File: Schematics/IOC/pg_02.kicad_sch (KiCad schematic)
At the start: 7 parts, among them U301 68020, U302 F260, U303 F260, U304 F51, U305 F02, U306 F20

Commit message: Align to grid
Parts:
- removed GB7: GB, symbol r1000:GB
- removed U301: 68020, symbol r1000:68020
- removed U302, U303: F260, symbol r1000:F260
- removed U304: F51, symbol r1000:F51
- removed U305: F02, symbol r1000:F02
- removed U306: F20, symbol r1000:F20
- added U: (no value), symbol r1000:GB
- added U: (no value), symbol r1000:F20
- added U (x2): (no value), symbol r1000:F260
- added U: (no value), symbol r1000:F51
- added U: (no value), symbol r1000:F02
- added U: (no value), symbol r1000:68020
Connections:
- net 68K.A0: now also U.C4 (A00)
- net 68K.A1: now also U.A2 (A01)
- net 68K.A10: now also U.B12 (A10)
- net 68K.A11: now also U.A12 (A11)
- net 68K.A12: now also U.C10 (A12)
- net 68K.A13: now also U.B11 (A13)
- net 68K.A14: now also U.A19 (A14)
- net 68K.A15: now also U.B10 (A15)
- net 68K.A16: now also U.C9 (A16)
- net 68K.A17: now also U.C8 (A17)
- net 68K.A18: now also U.B8 (A18)
- net 68K.A19: now also U.A8 (A19)
- net 68K.A2: now also U.E12 (A02)
- net 68K.A20: now also U.B7 (A20)
- net 68K.A21: now also U.C7 (A21)
- net 68K.A22: now also U.A7 (A22)
- net 68K.A23: now also U.A6 (A23)
- net 68K.A24: now also U.B6 (A24)
- net 68K.A25: now also U.C6 (A25)
- net 68K.A26: now also U.A5 (A26)
- net 68K.A27: now also U.B5 (A27)
- net 68K.A28: now also U.A4 (A28)
- net 68K.A29: now also U.C5 (A29)
- net 68K.A3: now also U.D13 (A03)
- net 68K.A30: now also U.B4 (A30)
- net 68K.A31: now also U.A3 (A31)
- net 68K.A4: now also U.D12 (A04)
- net 68K.A5: now also U.C13 (A05)
- net 68K.A6: now also U.B13 (A06)
- net 68K.A7: now also U.C12 (A07)
- net 68K.A8: now also U.A13 (A08)
- net 68K.A9: now also U.C11 (A09)
- net 68K.BERR~: now also U.7 (Q), U.J2 (BERR)
- net 68K.D0: now also U.K13 (D00)
- net 68K.D1: now also U.K12 (D01)
- net 68K.D10: now also U.M10 (D10)
- net 68K.D11: now also U.L9 (D11)
- net 68K.D12: now also U.N10 (D12)
- net 68K.D13: now also U.M9 (D13)
- net 68K.D14: now also U.N9 (D14)
- net 68K.D15: now also U.L8 (D15)
- net 68K.D16: now also U.M7 (D16)
- net 68K.D17: now also U.N6 (D17)
- net 68K.D18: now also U.M6 (D18)
- net 68K.D19: now also U.L6 (D19)
- net 68K.D2: now also U.L13 (D02)
- net 68K.D20: now also U.N5 (D20)
- net 68K.D21: now also U.M5 (D21)
- net 68K.D22: now also U.N4 (D22)
- net 68K.D23: now also U.L5 (D23)
- net 68K.D24: now also U.M4 (D24)
- net 68K.D25: now also U.N3 (D25)
- net 68K.D26: now also U.M3 (D26)
- net 68K.D27: now also U.L4 (D27)
- net 68K.D28: now also U.N2 (D28)
- net 68K.D29: now also U.M2 (D29)
- net 68K.D3: now also U.L12 (D03)
- net 68K.D30: now also U.L3 (D30)
- net 68K.D31: now also U.N1 (D31)
- net 68K.D4: now also U.M13 (D04)
- net 68K.D5: now also U.M12 (D05)
- net 68K.D6: now also U.M11 (D06)
- net 68K.D7: now also U.L10 (D07)
- net 68K.D8: now also U.N12 (D08)
- net 68K.D9: now also U.N11 (D09)
- net 68K.DSACK0~: now also U.5 (Q), U.H3 (DSACK0)
- net 68K.DSACK1~: now also U.5 (Q), U.J1 (DSACK1)
- net 68K.FC0: now also U.E1 (FC0)
- net 68K.FC1: now also U.F3 (FC1)
- net 68K.FC2: now also U.F2 (FC2)
- net 68K_RESET~: now also U.C1 (RESET)
- net AS~: now also U.L1 (AS)
- net CLK.2X.B5: now also U.C2 (CLK)
- net DBEN~: now also U.G3 (DBEN)
- net DEV.DSACK0: now also U.12 (D0)
- net DEV.DSACK1: now also U.12 (D0)
- net ECS~: now also U.G1 (ECS)
- net IACK_DSACK: now also U.1 (D2)
- net IO.BERRA~: now also U.1 (D0)
- net IO.BERRD~: now also U.2 (D1)
- net IO.DSACK: now also U.1 (D2)
- net IOP.BERR_EN: now also U.1 (A1)
- net IOP.PROT_BERR~: now also U.4 (D2)
- net IOP.RAM_DSACK: now also U.13 (D1), U.13 (D1)
- net IOP_CACHE_EN: now also U.1, U.H1 (CDIS)
- net IOP_HALT: now also U.3 (Q)
- net IPL0~: now also U.J12 (IPL0)
- net IPL1~: now also U.J13 (IPL1)
- net IPL2~: now also U.H12 (IPL2)
- net PD: now also U.2 (D3), U.2 (D3), U.3 (D4), U.3 (D4)
- net PU: now also U.1 (D0), U.2 (D1), U.3 (A3), U.4 (B1), U.5 (D3), U.6 (B3), U.A1 (BGACK), U.B3 (BR), U.H2 (AVEC), U.K2 (HALT)
- net RAM.PERR: now also U.2 (A2)
- net SIZ0: now also U.F1 (SIZ0)
- net SIZ1: now also U.G2 (SIZ1)
- net WR~: now also U.L2 (WR)
- new net: U.5 (B2), U.6 (Q)

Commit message: TYP/VAL busses
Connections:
- net PU: no longer U.K2 (HALT)
- no-connect marks 5 -> 6
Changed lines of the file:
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@@
   (junction (at 114.3 160.02) (diameter 0) (color 0 0 0 0)
   )
-  (junction (at 223.52 66.04) (diameter 0) (color 0 0 0 0)
-  )
   (junction (at 111.76 210.82) (diameter 0) (color 0 0 0 0)
   )
@@
   (junction (at 111.76 215.9) (diameter 0) (color 0 0 0 0)
   )
+  (no_connect (at 231.14 109.22))
   (no_connect (at 312.42 114.3))
   (no_connect (at 312.42 93.98))
@@
     (stroke (width 0) (type default))
   )
-  (wire (pts (xy 223.52 109.22) (xy 223.52 66.04))
-    (stroke (width 0) (type default))
-  )
   (bus (pts (xy 383.54 274.32) (xy 383.54 279.4))
     (stroke (width 0) (type default))
@@
     (stroke (width 0) (type default))
   )
-  (wire (pts (xy 231.14 109.22) (xy 223.52 109.22))
-    (stroke (width 0) (type default))
-  )

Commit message: IOC: dedup, clocks, dfsm
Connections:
- net CLK.2X.B5 renamed CLK.2X
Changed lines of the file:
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@@
     )
   )
-  (global_label "CLK.2X.B5" (shape input) (at 93.98 99.06 180) (fields_autoplaced)
+  (global_label "CLK.2X" (shape input) (at 93.98 99.06 180) (fields_autoplaced)
     (effects (font (size 2.54 2.54)) (justify right))
     (property "Intersheet References" "${INTERSHEET_REFS}" (id 0) (at 69.4206 98.9013 0)

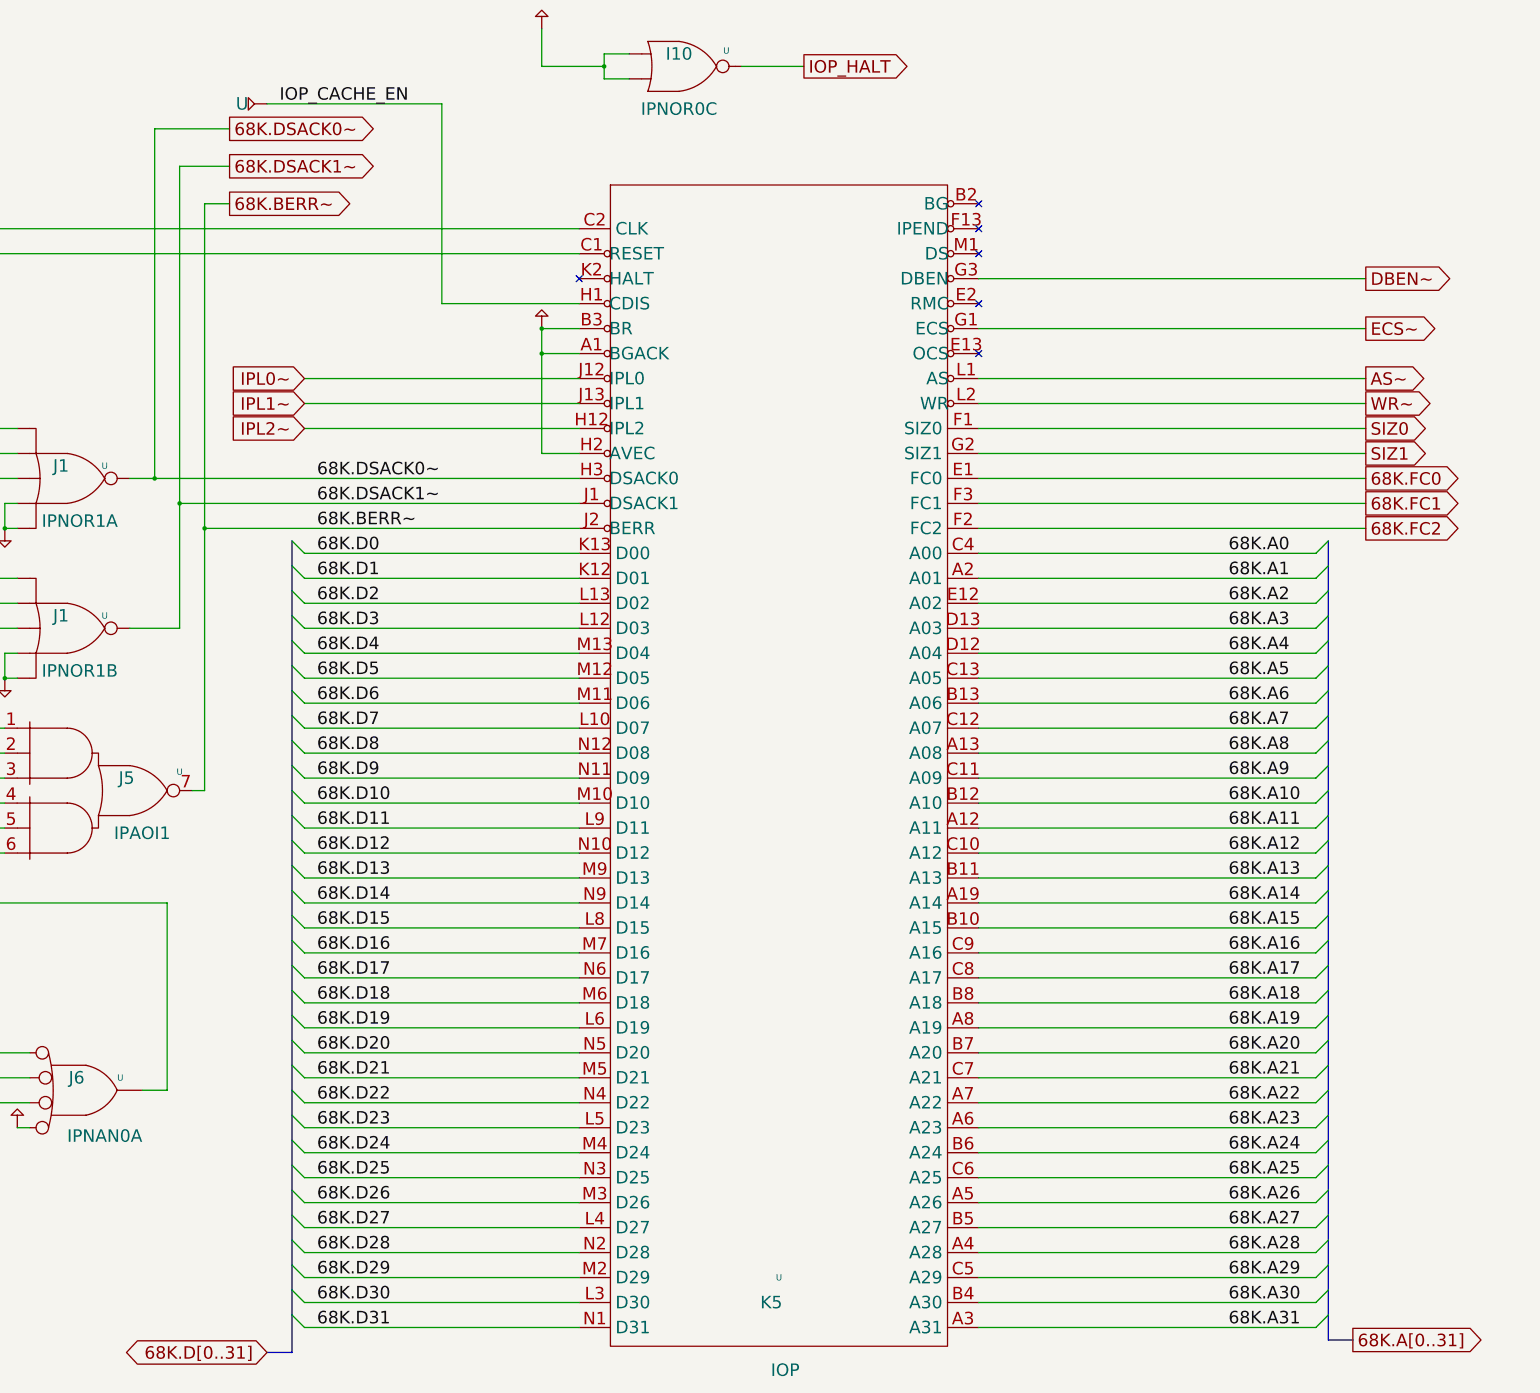
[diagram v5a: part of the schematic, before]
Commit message: IOC/RESHA cleanup, tested to 6 seconds (@c11)
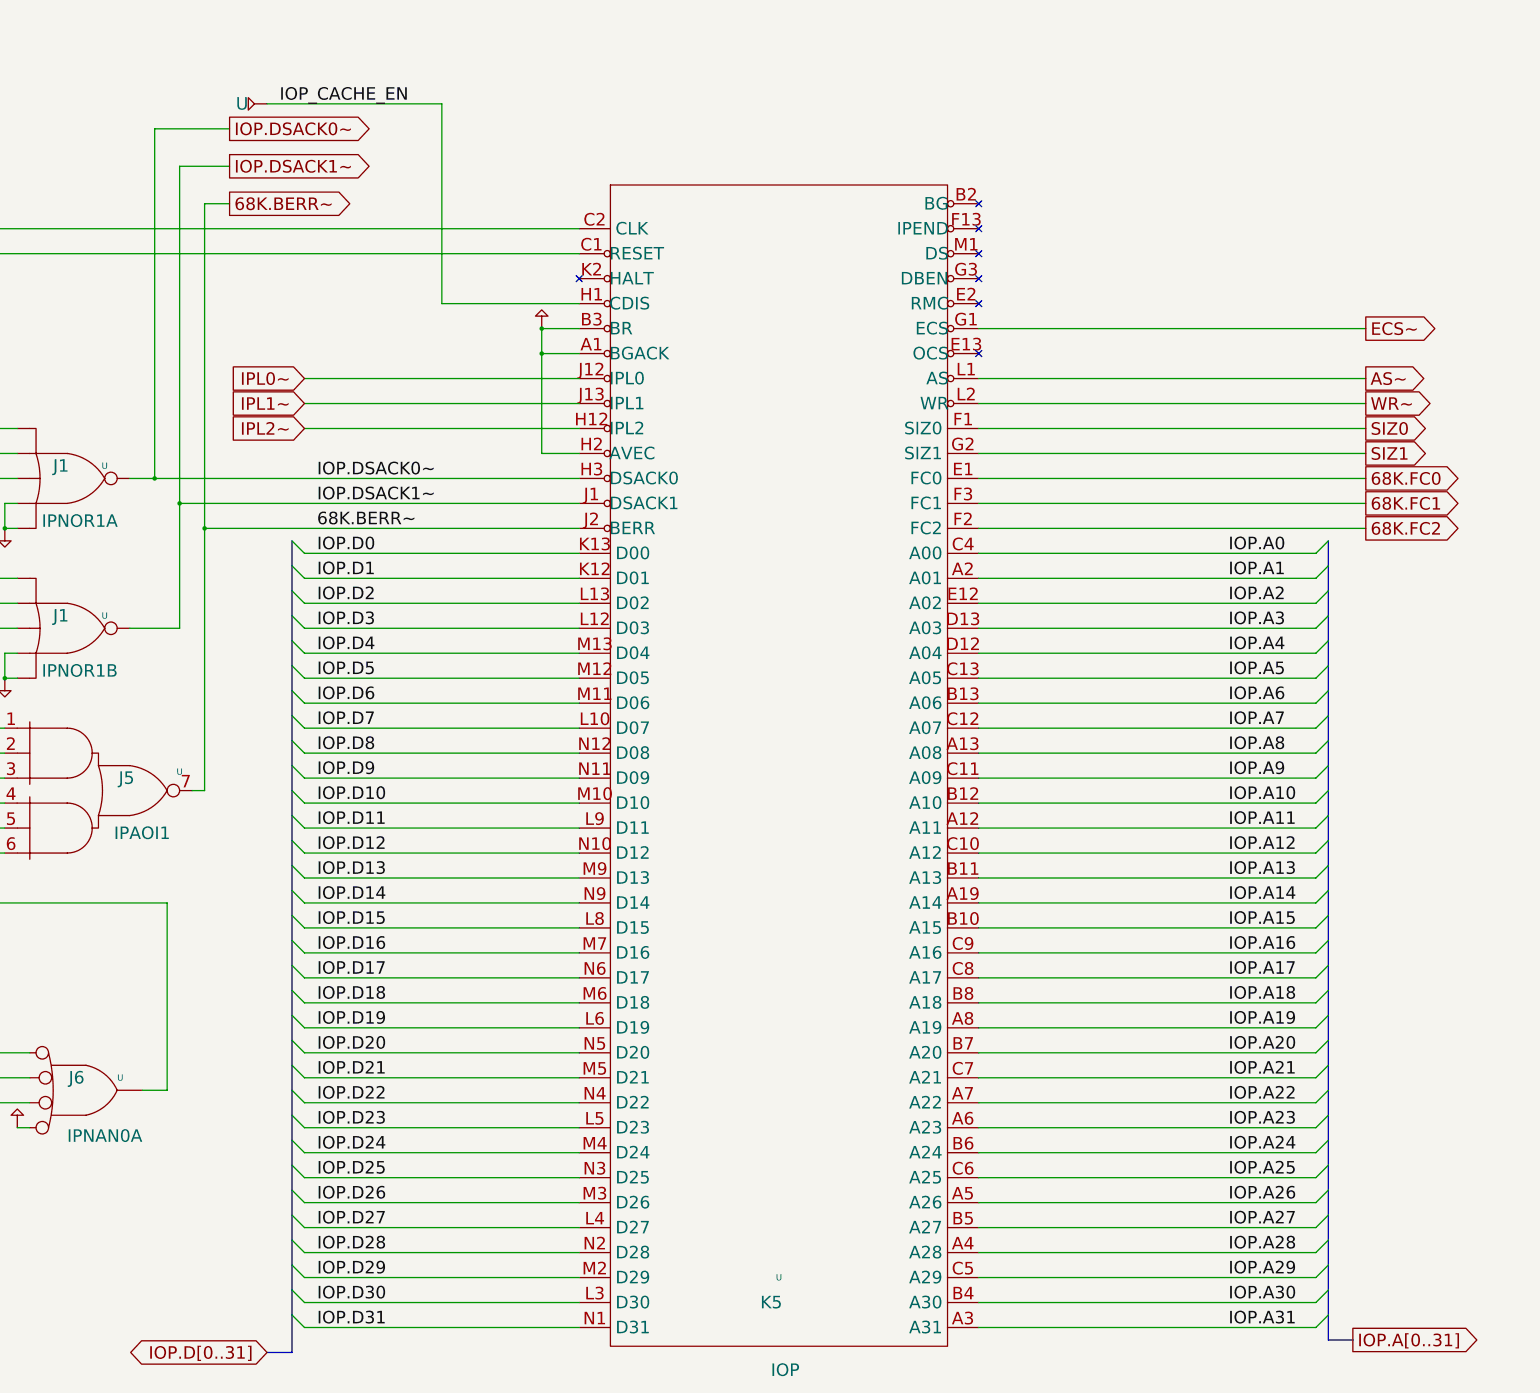
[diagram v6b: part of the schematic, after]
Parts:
- removed U: (no value), symbol r1000:F02
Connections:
- net 68K.A0 renamed IOP.A0
- net 68K.A1 renamed IOP.A1
- net 68K.A10 renamed IOP.A10
- net 68K.A11 renamed IOP.A11
- net 68K.A12 renamed IOP.A12
- net 68K.A13 renamed IOP.A13
- net 68K.A14 renamed IOP.A14
- net 68K.A15 renamed IOP.A15
- net 68K.A16 renamed IOP.A16
- net 68K.A17 renamed IOP.A17
- net 68K.A18 renamed IOP.A18
- net 68K.A19 renamed IOP.A19
- net 68K.A2 renamed IOP.A2
- net 68K.A20 renamed IOP.A20
- net 68K.A21 renamed IOP.A21
- net 68K.A22 renamed IOP.A22
- net 68K.A23 renamed IOP.A23
- net 68K.A24 renamed IOP.A24
- net 68K.A25 renamed IOP.A25
- net 68K.A26 renamed IOP.A26
- net 68K.A27 renamed IOP.A27
- net 68K.A28 renamed IOP.A28
- net 68K.A29 renamed IOP.A29
- net 68K.A3 renamed IOP.A3
- net 68K.A30 renamed IOP.A30
- net 68K.A31 renamed IOP.A31
- net 68K.A4 renamed IOP.A4
- net 68K.A5 renamed IOP.A5
- net 68K.A6 renamed IOP.A6
- net 68K.A7 renamed IOP.A7
- net 68K.A8 renamed IOP.A8
- net 68K.A9 renamed IOP.A9
- net 68K.D0 renamed IOP.D0
- net 68K.D1 renamed IOP.D1
- net 68K.D10 renamed IOP.D10
- net 68K.D11 renamed IOP.D11
- net 68K.D12 renamed IOP.D12
- net 68K.D13 renamed IOP.D13
- net 68K.D14 renamed IOP.D14
- net 68K.D15 renamed IOP.D15
- net 68K.D16 renamed IOP.D16
- net 68K.D17 renamed IOP.D17
- net 68K.D18 renamed IOP.D18
- net 68K.D19 renamed IOP.D19
- net 68K.D2 renamed IOP.D2
- net 68K.D20 renamed IOP.D20
- net 68K.D21 renamed IOP.D21
- net 68K.D22 renamed IOP.D22
- net 68K.D23 renamed IOP.D23
- net 68K.D24 renamed IOP.D24
- net 68K.D25 renamed IOP.D25
- net 68K.D26 renamed IOP.D26
- net 68K.D27 renamed IOP.D27
- net 68K.D28 renamed IOP.D28
- net 68K.D29 renamed IOP.D29
- net 68K.D3 renamed IOP.D3
- net 68K.D30 renamed IOP.D30
- net 68K.D31 renamed IOP.D31
- net 68K.D4 renamed IOP.D4
- net 68K.D5 renamed IOP.D5
- net 68K.D6 renamed IOP.D6
- net 68K.D7 renamed IOP.D7
- net 68K.D8 renamed IOP.D8
- net 68K.D9 renamed IOP.D9
- net 68K.DSACK0~ renamed IOP.DSACK0~
- net 68K.DSACK1~ renamed IOP.DSACK1~
- net DBEN~: no longer names the net of U.G3 (DBEN)
- no-connect marks 6 -> 7
